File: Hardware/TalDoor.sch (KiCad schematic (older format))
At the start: 65 parts, among them J1 SI-52003-F_RJ45, J2 Conn_01x02, J3 Conn_01x06_Male, J4 Conn_01x06_Male, P1 PocketBeagle, Q1 RK7002BM, Q2 BSS223PWH6327XTSA1, U1 DRV8837, U2 ENC28J60-I/SO, U3 PN532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

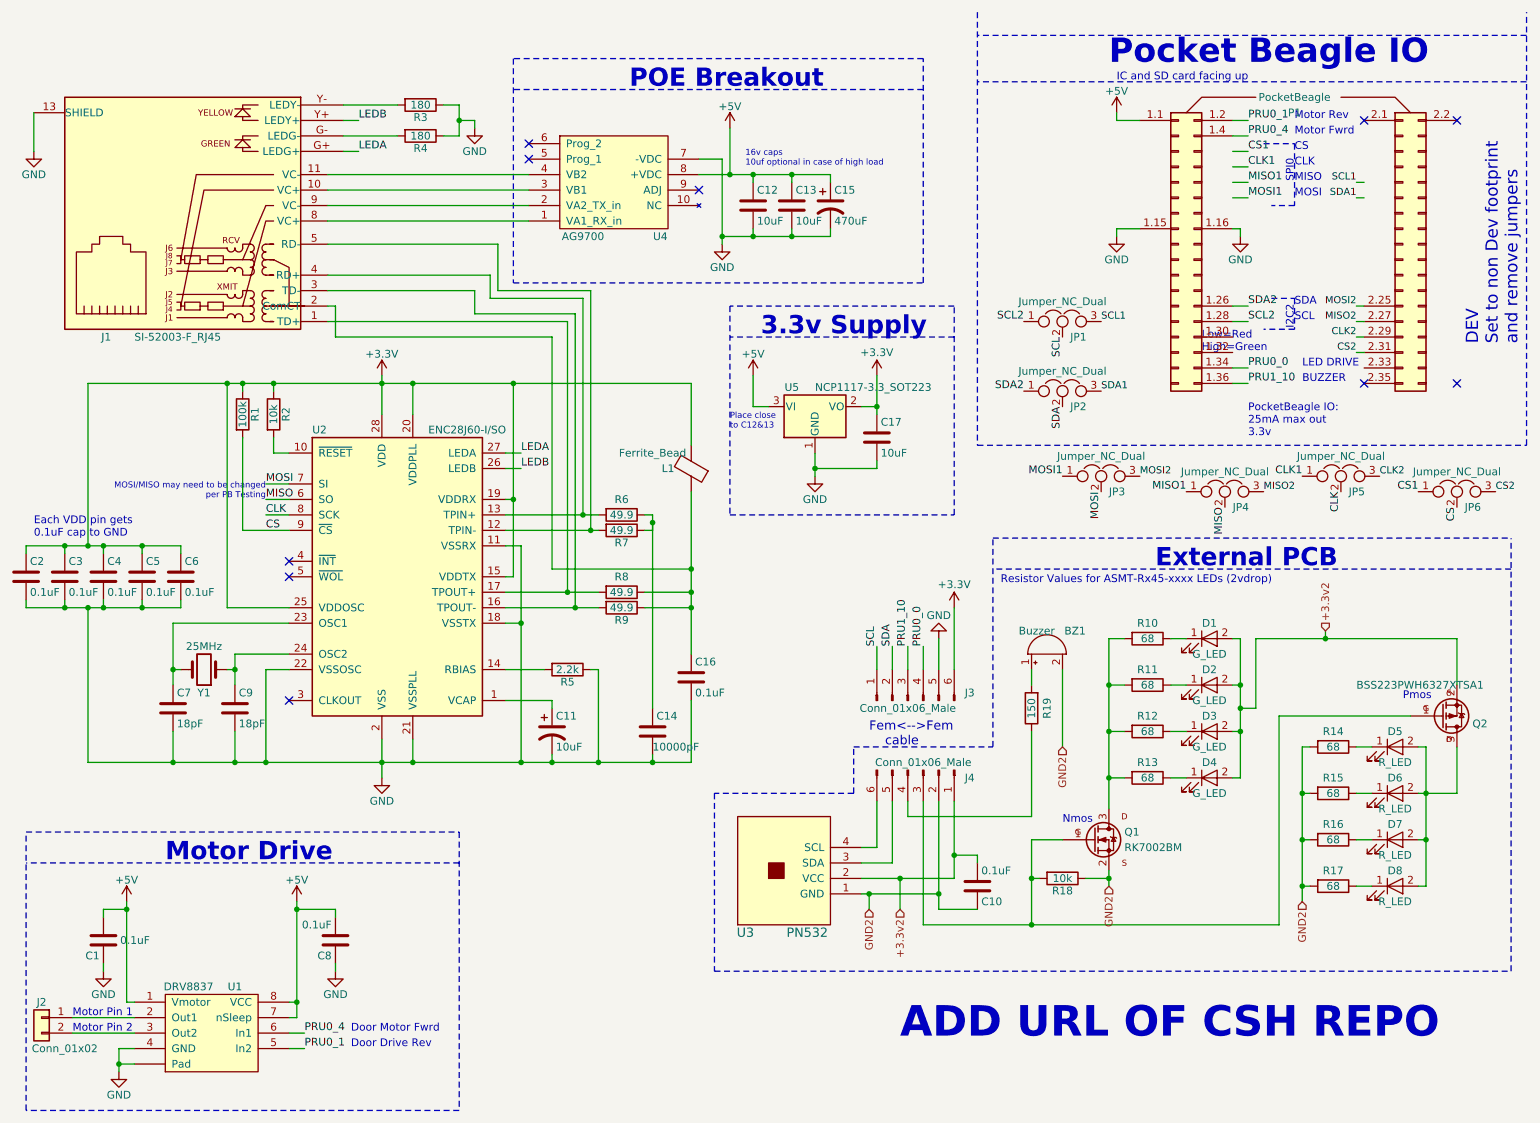
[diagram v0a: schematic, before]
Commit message: fixed ethernet module, SPI, I2c busses
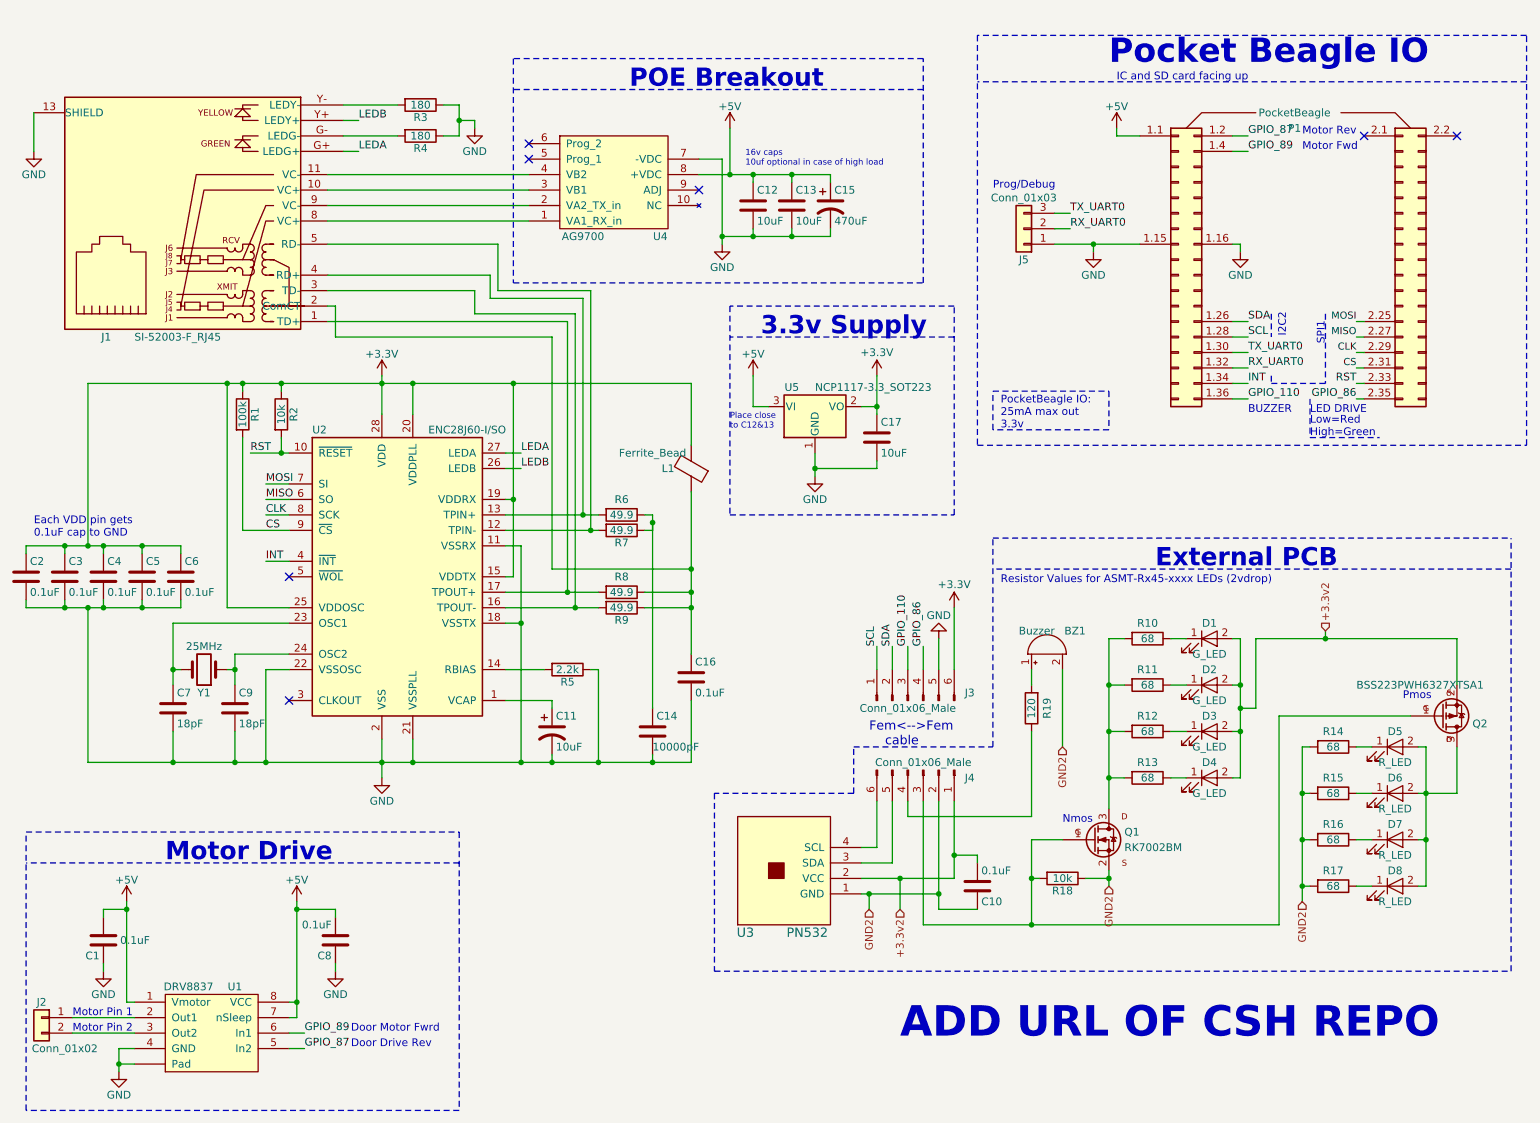
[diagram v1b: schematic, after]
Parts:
- removed JP1, JP2, JP3, JP4, JP5, JP6: Jumper_NC_Dual, Connectors:GS3, symbol Jumper_NC_Dual
- added J5: Conn_01x03, Pin_Headers:Pin_Header_Straight_1x03_Pitch2.54mm, symbol Conn_01x03
- P1: footprint TalDoor_Footprints:PocketBeagle_DEV_TalDoor -> TalDoor_Footprints:PocketBeagle_TalDoor
- R19: value 150 -> 120
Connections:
- net CLK2 is gone; now on net CLK: P1.2.29 (Pin_29)
- net CS2 is gone; now on net CS: P1.2.31 (Pin_31)
- net MISO2 is gone; now on net MISO: P1.2.27 (Pin_27)
- net MOSI2 is gone; now on net MOSI: P1.2.25 (Pin_25)
- net SCL2 is gone; now on net SCL: P1.1.28 (Pin_28)
- net SDA2 is gone; now on net SDA: P1.1.26 (Pin_26)
- net GND: now also J5.1 (Pin_1)
- net RST: now reaches R2.2, U2.10 (~RESET)
- net RST: now also P1.2.33 (Pin_33)
- net INT: now reaches U2.4 (~INT)
- net INT: now also P1.1.34 (Pin_34)
- net TX_UART0: now reaches P1.1.30 (Pin_30)
- net TX_UART0: now also J5.3 (Pin_3)
- net RX_UART0: now reaches P1.1.32 (Pin_32)
- net RX_UART0: now also J5.2 (Pin_2)
- net GPIO_86: now reaches P1.2.35 (Pin_35)
- net GPIO_86: now also J3.4 (Pin_4)
- removed net PRU0_0: J3.4 (Pin_4), P1.1.34 (Pin_34)
- net PRU0_1 renamed GPIO_87
- net PRU0_4 renamed GPIO_89
- net PRU1_10 renamed GPIO_110
- no-connect marks 10 -> 7
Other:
- note added: "Motor Fwd"
- note added: "Prog/Debug"
- note added: "SPI1"
- note removed: "CLK"
- note removed: "CS"
- note removed: "DEV\nSet to non Dev footprint\nand remove jumpers\n"
- note removed: "MISO"
- note removed: "MOSI"
- note removed: "MOSI/MISO may need to be changed\nper PB Testing"
- note removed: "Motor Fwrd"
- note removed: "SCL"
- note removed: "SDA"
- note removed: "SPI0"
- moved on the sheet: P1, R2

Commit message: updated BOM
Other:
- note added: "x"
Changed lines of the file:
@@
 Sheet 1 1
 Title "TalDoor Schematic"
-Date "2018-03-09"
-Rev "1.1"
+Date "2018-04-08"
+Rev "1.2"
 Comp "Spencer Kulbacki - Computer Science House"
 Comment1 "NFC Door lock hardware with POE support for the Pocket Beagle Devboard"
@@
 Text Notes 6950 1650 0    50   ~ 0
 Prog/Debug
+Wire Notes Line
+	8350 1500 8600 1500
+Text Notes 8600 1550 0    50   ~ 0
+x
 $EndSCHEMATC
